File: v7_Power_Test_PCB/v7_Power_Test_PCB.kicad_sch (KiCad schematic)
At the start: 0 parts

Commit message: update fuel gauge
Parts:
- added BT101, BT102: Battery_Cell, symbol Device:Battery_Cell
- added C1001, C101, C102, C105, C107, C108, C133, C136, C139: 0.1u, symbol Device:C
- added C1002, C114, C115, C126, C128: 1u, symbol Device:C
- added C1003: 10n, symbol Device:C
- added C104, C109: 4.3n, symbol Device:C
- added C110, C113, C122, C123: 100n, symbol Device:C
- added C111, C112, C125: 10u, symbol Device:C
- added C116: 100nF, symbol Device:C
- added C117, C118, C121, C129, C130, C131, C140: 47u, symbol Device:C
- added C119: 47p, symbol Device:C
- added C120: 1n, symbol Device:C
- added C124: 330u, symbol Device:C
- added C127: 4.7u, symbol Device:C
- added C132: 560u, symbol Device:C
- added C134: 150p, symbol Device:C
- added C135: 18n, symbol Device:C
- added C137, C138: 22u, symbol Device:C
- added D101, D102: D_TVS, ESD5451N2:DFN1006-2L_TWS, symbol Device:D_TVS
- added J101: Conn_01x02_Pin, symbol Connector:Conn_01x02_Pin
- added L101: 1u, symbol Device:L
- added L102: 4.7u, symbol Device:L
- added L103: 220n, symbol Device:L
- added R1001: 10m, symbol Device:R
- added R101, R102, R120, R121, R129, R130, R134, R142, R149, R150: 0, symbol Device:R
- added R106, R122: 470k, symbol Device:R
- added R107, R123: 47k, symbol Device:R
- added R110, R124: 82.5k, symbol Device:R
- added R111, R125: 27.4k, symbol Device:R
- added R112, R126, R136: 10k, symbol Device:R
- added R113, R127, R152: 205k, symbol Device:R
- added R115, R128: 576, symbol Device:R
- added R131: 267k, symbol Device:R
- added R132: 8.2k, symbol Device:R
- added R133, R138: 5k, symbol Device:R
- added R135: 24k, symbol Device:R
- added R137: 220k, symbol Device:R
- added R139: 23.7k, symbol Device:R
- added R140: 69.8k, symbol Device:R
- added R141: 124k, symbol Device:R
- added R143: 162k, symbol Device:R
- added R144: 102k, symbol Device:R
- added R145: 24.9k, symbol Device:R
- added R146, R151: 100k, symbol Device:R
- added R147: 9.53k, symbol Device:R
- added R148: 12.1k, symbol Device:R
- added TH1001: Thermistor_NTC, Resistor_SMD:R_0201_0603Metric_Pad0.64x0.40mm_HandSolder, symbol Device:Thermistor_NTC
- added U1001: ~, Package_DFN_QFN:WDFN-12-1EP_3x3mm_P0.45mm_EP1.7x2.5mm, symbol RT9426:RT9426GQW
- added U101, U107, U112, U114: LTC4450AV-TRMPBF, LTC4450:05-08-1683_ADI, symbol LTC4450:LTC4450AV-TRMPBF
- added U102, U108: TPS22811LRPWR, TPS22811:IC_TPS22811LRPWR, symbol TPS22811LRPWR:TPS22811LRPWR
- added U103: SN74LVC1G32DBVR, SN74LVC1G32DBVR:SOT95P280X145-5N, symbol SN74LVC1G32DBVR:SN74LVC1G32DBVR
- added U105: SN74LVC1G14DBVR, SN74LVC1G14DBVR:SOT95P280X145-5N, symbol SN74LVC1G14DBVR:SN74LVC1G14DBVR
- added U106: SN74LVC1G08DBVR, SN74LVC1G08DBVR:SOT95P280X145-5N, symbol SN74LVC1G08DBVR:SN74LVC1G08DBVR
- added U109: TPS2121RUXR, TPS2121RUXR:RUX0012A, symbol TPS2121RUXR:TPS2121RUXR
- added U110: TPS61088RHLR, TPS61088RHLR:IC_TPS61088RHLR, symbol TPS61088RHLR:TPS61088RHLR
- added U111: XTPS55285VALR, TPS55285VALR:VAL0015A, symbol TPS55285VALR:XTPS55285VALR
- added U113: TPS62867RQYR, TPS62867RQYR:RQY0009A-MFG, symbol TPS62867RQYR:TPS62867RQYR
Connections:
- new net: C128.1, C129.1, C130.1, C131.1, C132.1, R144.2, U111.9 (VOUT), U112.16 (SHDN#), U112.2 (IN), U112.3 (IN), U112.4 (IN), U112.5 (IN), U112.6 (IN), U112.7 (IN)
- new net: R145.2, U111.1 (MODE)
- new net: R121.1, U107.10 (OUT), U107.11 (OUT), U107.12 (OUT), U107.13 (OUT), U107.8 (OUT), U107.9 (OUT)
- new net: R137.2, R140.1, U110.17 (FB)
- new net: R150.1, U114.10 (OUT), U114.11 (OUT), U114.12 (OUT), U114.13 (OUT), U114.8 (OUT), U114.9 (OUT)
- new net: R143.2, R146.1, U111.4 (EN_UVLO)
- new net: R101.2, R106.1, U102.5 (IN)
- new net: R106.2, R110.1, U102.1 (EN/UVLO)
- new net: R120.2, R122.1, U108.5 (IN)
- new net: R122.2, R124.1, U108.1 (EN/UVLO)
- new net: C114.1, C115.1, U110.1 (VCC)
- new net: C110.2, L101.2, R131.1, U110.4 (SW_7), U110.5 (SW_4), U110.6 (SW_5), U110.7 (SW_6)
- new net: R131.2, U110.3 (FSW)
- new net: R110.2, R113.1, U102.2 (~{EN}/OVLO)
- new net: R123.2, R125.1, U108.4 (PGTH)
- new net: C127.1, U111.13 (VCC)
- new net: R128.1, U108.9 (IMON)
- new net: C134.1, R148.2, U111.11 (COMP)
- new net: BT102.1 (+), R120.1
- new net: R144.1, R147.2, U111.10 (FB_INT_N)
- new net: C1003.1, TH1001.1, U1001.5 (VPTS)
- new net: C1003.2, TH1001.2, U1001.9 (TS)
- new net: BT101.1 (+), R101.1
- new net: C119.1, R139.1, U110.18 (COMP)
- new net: R102.1, U101.10 (OUT), U101.11 (OUT), U101.12 (OUT), U101.13 (OUT), U101.8 (OUT), U101.9 (OUT)
- new net: R149.2, R151.1, U113.3 (VIN), U113.4 (EN)
- new net: R134.2, U109.2 (IN2)
- new net: R152.1, U113.6 (VSET_MODE)
- new net: C110.1, U110.8 (BOOT)
- new net: C104.1, U102.7 (DVDT)
- new net: C135.1, R148.1
- new net: C133.1, R142.1, U112.10 (OUT), U112.11 (OUT), U112.12 (OUT), U112.13 (OUT), U112.8 (OUT), U112.9 (OUT)
- new net: L103.1, U113.7 (SW)
- new net: R124.2, R127.1, U108.2 (~{EN}/OVLO)
- new net: C109.1, U108.7 (DVDT)
- new net: C123.1, L102.2, U111.8 (SW2)
- new net: C123.2, U111.14 (BOOT2)
- new net: C120.1, R139.2
- new net: C122.2, U111.15 (BOOT1)
- new net: C122.1, L102.1, U111.6 (SW1)
- new net: R130.1, U109.1 (OUT), U109.8 (OUT)
- new net: R135.1, U109.10 (ILM)
- new net: C116.1, U109.11 (SS)
- new net: R129.2, U109.7 (IN1)
- new net: U105.4 (Y), U106.1 (A)
- new net: R141.1, U110.19 (ILIM)
- new net: R107.2, R111.1, U102.4 (PGTH)
- new net: C121.1, U110.10 (SS)
- new net: R115.1, U102.9 (IMON)
- new net 5V_IN: C140.1, J101.1 (Pin_1), R129.1, R132.2, R149.1
- new net 5V_MUX_STATUS: U109.9 (ST)
- new net BATTERY_PACK_OUT: C1001.1, C1002.1, C102.1, C105.1, C108.1, C111.1, C112.1, C113.1, C124.1, C125.1, C126.1, L101.1, R102.2, R121.2, U1001.3 (VDD/VBAT), U1001.4 (VBATS), U103.5 (VCC), U110.9 (VIN), U111.5 (VIN)
- new net BATTERY_PG: U103.4, U106.2 (B), U110.2 (EN)
- new net BAT_3V3_EN: R143.1, U106.4 (Y)
- new net BAT_5V: C117.1, C118.1, R134.1, R136.1, R137.1, U110.14 (VOUT_16), U110.15 (VOUT_14), U110.16 (VOUT_15)
- new net CP2: R136.2, R138.2, U109.3 (CP2)
- new net ETH_3V3: C137.1, C138.1, C139.1, L103.2, U113.8 (VOS), U113.9 (FB), U114.16 (SHDN#), U114.2 (IN), U114.3 (IN), U114.4 (IN), U114.5 (IN), U114.6 (IN), U114.7 (IN)
- new net ETH_3V3_PG: R151.2, U105.2 (A), U113.5 (PG)
- new net FUEL_GAUGE_ALERT: U1001.12 (nALERT)
- new net FUEL_GAUGE_SCL: U1001.11 (SCL)
- new net FUEL_GAUGE_SDA: U1001.10 (SDA)
- new net GND: C1001.2, C111.2, C112.2, C113.2, C114.2, C115.2, C116.2, C117.2, C118.2, C119.2, C120.2, C121.2, C124.2, C125.2, C126.2, C127.2, C128.2, C129.2, C130.2, C131.2, C132.2, C133.2, C134.2, C135.2, C136.2, C137.2, C138.2, C139.2, C140.2, J101.2 (Pin_2), R1001.2, R133.2, R135.2, R138.1, R140.2, R141.2, R145.1, R146.2, R147.1, R152.2, U1001.6 (VSS), U1001.8 (CSN), U1001.EP, U103.3 (GND), U105.3 (GND), U106.3 (GND), U109.12 (GND), U109.4 (OV2), U109.5 (OV1), U110.11 (NC_11), U110.20 (AGND), U110.21 (PGND), U110.22 (PGND__1), U110.23 (PGND__2), U110.24 (PGND__3), U110.25 (PGND__4), U110.26 (PGND__5), U110.27 (PGND__6), U110.28 (PGND__7), U110.29 (PGND__8), U111.12 (AGND), U111.7 (PGND), U112.1 (VCC), U112.14 (GND), U112.15 (STATUS), U113.1 (AGND), U113.2 (PGND), U114.1 (VCC), U114.14 (GND), U114.15 (STATUS)
- new net LOAD_OUT_1: C101.1, D101.2 (A2), R107.1, R112.1, U101.16 (SHDN#), U101.2 (IN), U101.3 (IN), U101.4 (IN), U101.5 (IN), U101.6 (IN), U101.7 (IN), U102.6 (OUT)
- new net LOAD_OUT_2: C107.1, D102.2 (A2), R123.1, R126.1, U107.16 (SHDN#), U107.2 (IN), U107.3 (IN), U107.4 (IN), U107.5 (IN), U107.6 (IN), U107.7 (IN), U108.6 (OUT)
- new net LOAD_PG_1: R112.2, U102.3 (PG), U103.1
- new net LOAD_PG_2: R126.2, U103.2, U108.3 (PG)
- new net PACK_GND: BT101.2 (-), BT102.2 (-), C1002.2, C101.2, C102.2, C104.2, C105.2, C107.2, C108.2, C109.2, D101.1 (A1), D102.1 (A1), R1001.1, R111.2, R113.2, R115.2, R125.2, R127.2, R128.2, U1001.2 (VBATG), U1001.7 (CSP), U101.1 (VCC), U101.14 (GND), U101.15 (STATUS), U102.8 (GND), U107.1 (VCC), U107.14 (GND), U107.15 (STATUS), U108.8 (GND)
- new net PR1: R132.1, R133.1, U109.6 (PR1)
- new net VCC3V3_SYS: C136.1, R142.2, R150.2, U105.5 (VCC), U106.5 (VCC)
- new net VCC5V_SYS: R130.2
- no-connect marks 0 -> 1
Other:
- note added: "5V Boost EN when good battery"
- note added: "AND"
- note added: "Battery 3.3V Buck EN when good battery and no POE"
- note added: "Battery Management"
- note added: "Battery to 3.3V"
- note added: "Battery to 5V"
- note added: "Battery/Ethernet 5V Switchover"
- note added: "ESP FOR READING FUEL GAUGE"
- note added: "NOT"
- note added: "NOTE: CHECK FOOTPRINT DIMENSIONS W DATASHEET"
- note added: "PoE to 3.3V"
- note added: "Power Sequencing/EN Logic"
- note added: "RESISTORS FOR LOAD SIMULATION"
- note added: "STATUS indication unused"

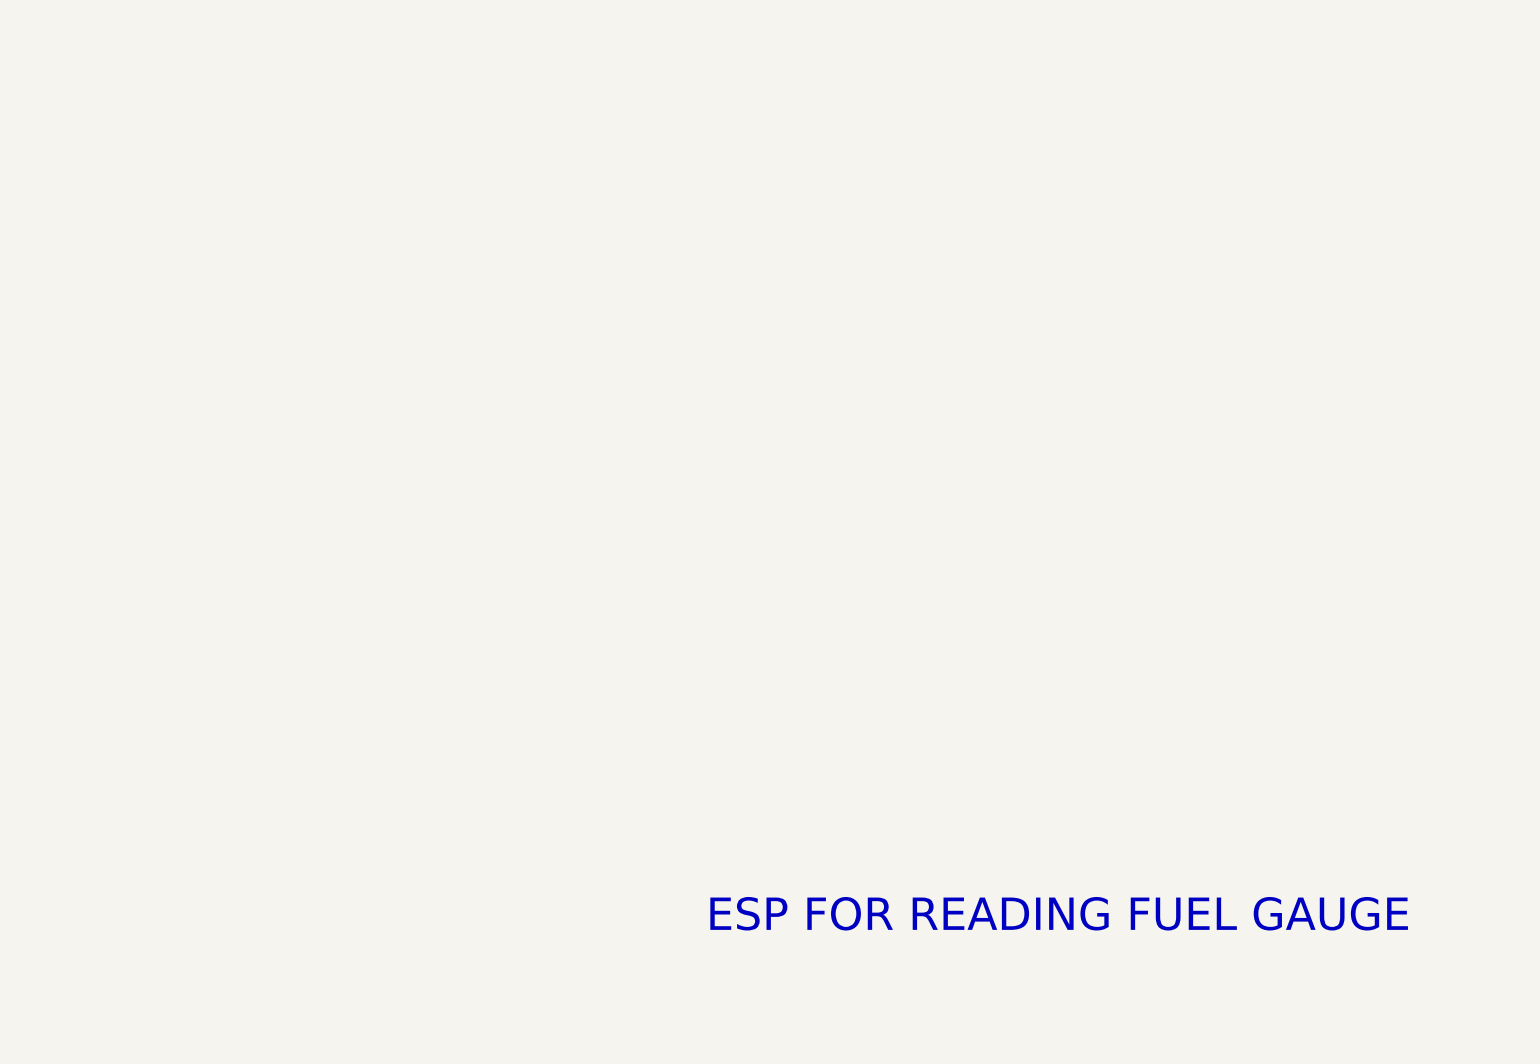
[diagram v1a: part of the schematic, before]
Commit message: add ESP32
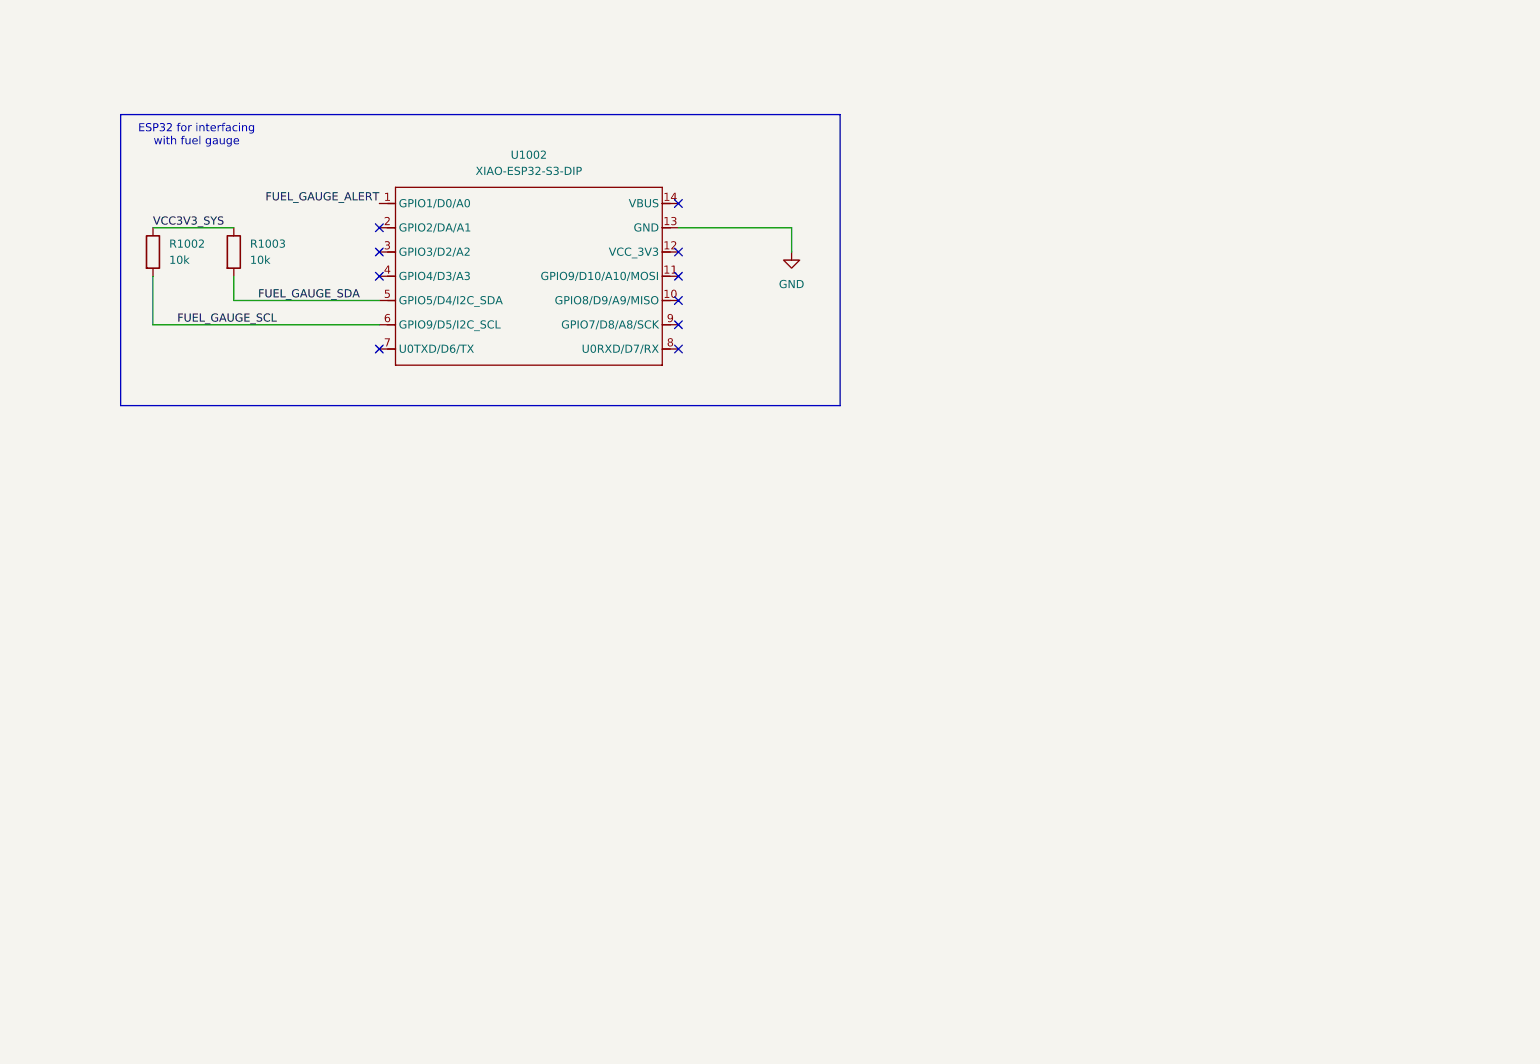
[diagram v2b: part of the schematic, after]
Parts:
- added R1002, R1003: 10k, symbol Device:R
- added U1002: XIAO-ESP32-S3-DIP, XIAO-ESP32S3:XIAO-ESP32S3-DIP, symbol XIAOESP32S3S:XIAO-ESP32-S3-DIP
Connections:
- net FUEL_GAUGE_ALERT: now also U1002.1 (GPIO1/D0/A0)
- net FUEL_GAUGE_SCL: now also R1002.2, U1002.6 (GPIO9/D5/I2C_SCL)
- net FUEL_GAUGE_SDA: now also R1003.2, U1002.5 (GPIO5/D4/I2C_SDA)
- net GND: now also U1002.13 (GND)
- net VCC3V3_SYS: now also R1002.1, R1003.1
- no-connect marks 1 -> 11
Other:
- note added: "ESP32 for interfacing with fuel gauge"
- note removed: "ESP FOR READING FUEL GAUGE"

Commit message: finish schematic and footprint assignments
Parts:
- removed BT101, BT102: Battery_Cell, symbol Device:Battery_Cell
- removed C124: 330u, symbol Device:C
- added BT1, BT2, BT3, BT4: 246, 246:BAT_246, symbol 246:246
- added C1, C10, C11, C2: 100n, Capacitor_SMD:C_0603_1608Metric_Pad1.08x0.95mm_HandSolder, symbol Device:C
- added C29: 330u, UCD0J331MCL1GS:PCAP_6.3x7.7-ELECT_NCA, symbol Device:C_Polarized_US
- added R35, R43: 50, Resistor_SMD:R_1206_3216Metric_Pad1.30x1.75mm_HandSolder, symbol Device:R
- added R36, R37, R38: AP725 5R F, AP725_5R_F:RES_AP725_OHM, symbol AP725_5R_F:AP725_5R_F
- added R39, R40, R41, R42: 3.3, CPA2512Q3R30FS_T10:RES_2512_SUS, symbol Device:R
- C12: renamed from C107; value 0.1u -> 100n; footprint (none) -> Capacitor_SMD:C_0603_1608Metric_Pad1.08x0.95mm_HandSolder
- C13: renamed from C108; value 0.1u -> 100n; footprint (none) -> Capacitor_SMD:C_0603_1608Metric_Pad1.08x0.95mm_HandSolder
- C14: renamed from C109; footprint (none) -> Capacitor_SMD:C_0603_1608Metric_Pad1.08x0.95mm_HandSolder
- C15: renamed from C110; footprint (none) -> Capacitor_SMD:C_0603_1608Metric_Pad1.08x0.95mm_HandSolder
- C16: renamed from C111; footprint (none) -> Capacitor_SMD:C_0603_1608Metric_Pad1.08x0.95mm_HandSolder
- C17: renamed from C112; footprint (none) -> Capacitor_SMD:C_0603_1608Metric_Pad1.08x0.95mm_HandSolder
- C18: renamed from C113; footprint (none) -> Capacitor_SMD:C_0603_1608Metric_Pad1.08x0.95mm_HandSolder
- C19: renamed from C114; footprint (none) -> Capacitor_SMD:C_0603_1608Metric_Pad1.08x0.95mm_HandSolder
- C20: renamed from C115; footprint (none) -> Capacitor_SMD:C_0603_1608Metric_Pad1.08x0.95mm_HandSolder
- C21: renamed from C116; value 100nF -> 100n; footprint (none) -> Capacitor_SMD:C_0603_1608Metric_Pad1.08x0.95mm_HandSolder
- C22: renamed from C117; footprint (none) -> Capacitor_SMD:C_0603_1608Metric_Pad1.08x0.95mm_HandSolder
- C23: renamed from C118; footprint (none) -> Capacitor_SMD:C_0603_1608Metric_Pad1.08x0.95mm_HandSolder
- C24: renamed from C119; footprint (none) -> Capacitor_SMD:C_0603_1608Metric_Pad1.08x0.95mm_HandSolder
- C25: renamed from C120; footprint (none) -> Capacitor_SMD:C_0603_1608Metric_Pad1.08x0.95mm_HandSolder
- C26: renamed from C121; footprint (none) -> Capacitor_SMD:C_0603_1608Metric_Pad1.08x0.95mm_HandSolder
- C27: renamed from C122; footprint (none) -> Capacitor_SMD:C_0603_1608Metric_Pad1.08x0.95mm_HandSolder
- C28: renamed from C123; footprint (none) -> Capacitor_SMD:C_0603_1608Metric_Pad1.08x0.95mm_HandSolder
- C3: renamed from C101; value 0.1u -> 100n; footprint (none) -> Capacitor_SMD:C_0603_1608Metric_Pad1.08x0.95mm_HandSolder
- C30: renamed from C125; footprint (none) -> Capacitor_SMD:C_0603_1608Metric_Pad1.08x0.95mm_HandSolder
- C31: renamed from C126; footprint (none) -> Capacitor_SMD:C_0603_1608Metric_Pad1.08x0.95mm_HandSolder
- C32: renamed from C127; footprint (none) -> Capacitor_SMD:C_0603_1608Metric_Pad1.08x0.95mm_HandSolder
- C33: renamed from C128; footprint (none) -> Capacitor_SMD:C_0603_1608Metric_Pad1.08x0.95mm_HandSolder
- C34: renamed from C129; footprint (none) -> Capacitor_SMD:C_0603_1608Metric_Pad1.08x0.95mm_HandSolder
- C35: renamed from C130; footprint (none) -> Capacitor_SMD:C_0603_1608Metric_Pad1.08x0.95mm_HandSolder
- C36: renamed from C131; footprint (none) -> Capacitor_SMD:C_0603_1608Metric_Pad1.08x0.95mm_HandSolder
- C37: renamed from C132; footprint (none) -> 16SVPF560M:CAP_16SVPF560M
- C38: renamed from C133; value 0.1u -> 100n; footprint (none) -> Capacitor_SMD:C_0603_1608Metric_Pad1.08x0.95mm_HandSolder
- C39: renamed from C134; footprint (none) -> Capacitor_SMD:C_0603_1608Metric_Pad1.08x0.95mm_HandSolder
- C4: renamed from C102; value 0.1u -> 100n; footprint (none) -> Capacitor_SMD:C_0603_1608Metric_Pad1.08x0.95mm_HandSolder
- C40: renamed from C135; footprint (none) -> Capacitor_SMD:C_0603_1608Metric_Pad1.08x0.95mm_HandSolder
- C41: renamed from C136; value 0.1u -> 100n; footprint (none) -> Capacitor_SMD:C_0603_1608Metric_Pad1.08x0.95mm_HandSolder
- C42: renamed from C137; footprint (none) -> Capacitor_SMD:C_0603_1608Metric_Pad1.08x0.95mm_HandSolder
- C43: renamed from C138; footprint (none) -> Capacitor_SMD:C_0603_1608Metric_Pad1.08x0.95mm_HandSolder
- C44: renamed from C139; value 0.1u -> 100n; footprint (none) -> Capacitor_SMD:C_0603_1608Metric_Pad1.08x0.95mm_HandSolder
- C45: renamed from C140; footprint (none) -> Capacitor_SMD:C_0603_1608Metric_Pad1.08x0.95mm_HandSolder
- C5: renamed from C1001; value 0.1u -> 100n; footprint (none) -> Capacitor_SMD:C_0603_1608Metric_Pad1.08x0.95mm_HandSolder
- C6: renamed from C105; value 0.1u -> 100n; footprint (none) -> Capacitor_SMD:C_0603_1608Metric_Pad1.08x0.95mm_HandSolder
- C7: renamed from C1003; footprint (none) -> Capacitor_SMD:C_0603_1608Metric_Pad1.08x0.95mm_HandSolder
- C8: renamed from C1002; footprint (none) -> Capacitor_SMD:C_0603_1608Metric_Pad1.08x0.95mm_HandSolder
- C9: renamed from C104; footprint (none) -> Capacitor_SMD:C_0603_1608Metric_Pad1.08x0.95mm_HandSolder
- J1: renamed from J101; footprint (none) -> Connector_PinHeader_2.54mm:PinHeader_1x02_P2.54mm_Horizontal
- L1: renamed from L101; footprint (none) -> BMRF001010401R0MD1:IND_BMRF001010401_PUL
- L2: renamed from L102; footprint (none) -> ETQ_P4M4R7KVC:IND_PCC-M1040LP_PAN
- L3: renamed from L103; footprint (none) -> IHLP2020CZERR22M8A:IND_IHLP-2020CZ-8A_VIS
- R1: renamed from R101; footprint (none) -> Resistor_SMD:R_0805_2012Metric_Pad1.20x1.40mm_HandSolder
- R10: renamed from R1001; footprint (none) -> Resistor_SMD:R_2512_6332Metric_Pad1.40x3.35mm_HandSolder
- R11: renamed from R120; footprint (none) -> Resistor_SMD:R_0805_2012Metric_Pad1.20x1.40mm_HandSolder
- R12: renamed from R121; footprint (none) -> Resistor_SMD:R_0805_2012Metric_Pad1.20x1.40mm_HandSolder
- R13: renamed from R122; footprint (none) -> Resistor_SMD:R_0603_1608Metric_Pad0.98x0.95mm_HandSolder
- R14: renamed from R123; footprint (none) -> Resistor_SMD:R_0603_1608Metric_Pad0.98x0.95mm_HandSolder
- R15: renamed from R124; footprint (none) -> Resistor_SMD:R_0603_1608Metric_Pad0.98x0.95mm_HandSolder
- R16: renamed from R125; footprint (none) -> Resistor_SMD:R_0603_1608Metric_Pad0.98x0.95mm_HandSolder
- R17: renamed from R126; footprint (none) -> Resistor_SMD:R_0603_1608Metric_Pad0.98x0.95mm_HandSolder
- R18: renamed from R127; footprint (none) -> Resistor_SMD:R_0603_1608Metric_Pad0.98x0.95mm_HandSolder
- R19: renamed from R128; footprint (none) -> Resistor_SMD:R_0603_1608Metric_Pad0.98x0.95mm_HandSolder
- R2: renamed from R102; footprint (none) -> Resistor_SMD:R_0805_2012Metric_Pad1.20x1.40mm_HandSolder
- R20: renamed from R1002; footprint (none) -> Resistor_SMD:R_0603_1608Metric_Pad0.98x0.95mm_HandSolder
- R21: renamed from R1003; footprint (none) -> Resistor_SMD:R_0603_1608Metric_Pad0.98x0.95mm_HandSolder
- R22: renamed from R129; footprint (none) -> Resistor_SMD:R_0805_2012Metric_Pad1.20x1.40mm_HandSolder
- R23: renamed from R130; footprint (none) -> Resistor_SMD:R_0805_2012Metric_Pad1.20x1.40mm_HandSolder
- R24: renamed from R131; footprint (none) -> Resistor_SMD:R_0603_1608Metric_Pad0.98x0.95mm_HandSolder
- R25: renamed from R132; footprint (none) -> Resistor_SMD:R_0603_1608Metric_Pad0.98x0.95mm_HandSolder
- R26: renamed from R133; footprint (none) -> Resistor_SMD:R_0603_1608Metric_Pad0.98x0.95mm_HandSolder
- R27: renamed from R134; footprint (none) -> Resistor_SMD:R_0805_2012Metric_Pad1.20x1.40mm_HandSolder
- R28: renamed from R135; footprint (none) -> Resistor_SMD:R_0603_1608Metric_Pad0.98x0.95mm_HandSolder
- R29: renamed from R136; footprint (none) -> Resistor_SMD:R_0603_1608Metric_Pad0.98x0.95mm_HandSolder
- R3: renamed from R106; footprint (none) -> Resistor_SMD:R_0603_1608Metric_Pad0.98x0.95mm_HandSolder
- R30: renamed from R137; footprint (none) -> Resistor_SMD:R_0603_1608Metric_Pad0.98x0.95mm_HandSolder
- R31: renamed from R138; footprint (none) -> Resistor_SMD:R_0603_1608Metric_Pad0.98x0.95mm_HandSolder
- R32: renamed from R139; footprint (none) -> Resistor_SMD:R_0603_1608Metric_Pad0.98x0.95mm_HandSolder
- R33: renamed from R140; footprint (none) -> Resistor_SMD:R_0603_1608Metric_Pad0.98x0.95mm_HandSolder
- R34: renamed from R141; footprint (none) -> Resistor_SMD:R_0603_1608Metric_Pad0.98x0.95mm_HandSolder
- R4: renamed from R107; footprint (none) -> Resistor_SMD:R_0603_1608Metric_Pad0.98x0.95mm_HandSolder
- R44: renamed from R142; footprint (none) -> Resistor_SMD:R_0805_2012Metric_Pad1.20x1.40mm_HandSolder
- R45: renamed from R143; footprint (none) -> Resistor_SMD:R_0603_1608Metric_Pad0.98x0.95mm_HandSolder
- R46: renamed from R144; footprint (none) -> Resistor_SMD:R_0603_1608Metric_Pad0.98x0.95mm_HandSolder
- R47: renamed from R145; footprint (none) -> Resistor_SMD:R_0603_1608Metric_Pad0.98x0.95mm_HandSolder
- R48: renamed from R146; footprint (none) -> Resistor_SMD:R_0603_1608Metric_Pad0.98x0.95mm_HandSolder
- R49: renamed from R147; footprint (none) -> Resistor_SMD:R_0603_1608Metric_Pad0.98x0.95mm_HandSolder
- R5: renamed from R110; footprint (none) -> Resistor_SMD:R_0603_1608Metric_Pad0.98x0.95mm_HandSolder
- R50: renamed from R148; footprint (none) -> Resistor_SMD:R_0603_1608Metric_Pad0.98x0.95mm_HandSolder
- R51: renamed from R149; footprint (none) -> Resistor_SMD:R_0805_2012Metric_Pad1.20x1.40mm_HandSolder
- R52: renamed from R150; footprint (none) -> Resistor_SMD:R_0805_2012Metric_Pad1.20x1.40mm_HandSolder
- R53: renamed from R151; footprint (none) -> Resistor_SMD:R_0603_1608Metric_Pad0.98x0.95mm_HandSolder
- R54: renamed from R152; footprint (none) -> Resistor_SMD:R_0603_1608Metric_Pad0.98x0.95mm_HandSolder
- R6: renamed from R111; footprint (none) -> Resistor_SMD:R_0603_1608Metric_Pad0.98x0.95mm_HandSolder
- R7: renamed from R112; footprint (none) -> Resistor_SMD:R_0603_1608Metric_Pad0.98x0.95mm_HandSolder
- R8: renamed from R113; footprint (none) -> Resistor_SMD:R_0603_1608Metric_Pad0.98x0.95mm_HandSolder
- R9: renamed from R115; footprint (none) -> Resistor_SMD:R_0603_1608Metric_Pad0.98x0.95mm_HandSolder
- renumbered D101 to D1, D102 to D2, TH1001 to TH1, U101 to U1, U109 to U10, U110 to U11, U111 to U12, U112 to U13, U113 to U14, U114 to U15, U102 to U2, U1001 to U3, U103 to U4, U105 to U5, U106 to U6, U107 to U7, U108 to U8, U1002 to U9
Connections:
- net 5V_MUX_STATUS: now also U9.2 (GPIO2/DA/A1)
- net BATTERY_PACK_OUT: now also C29.1
- net GND: now also C29.2, R35.2, R36.1, R37.1, R38.1, R39.2, R40.2, R41.2, R42.2, R43.2
- net PACK_GND: now also BT2.1_1, BT2.1_2, BT4.1_1, BT4.1_2, C1.2, C10.2, C11.2, C2.2
- net VCC3V3_SYS: now also R39.1, R40.1, R41.1, R42.1, R43.1
- net VCC5V_SYS: now also R37.2
- net at R1.2, R3.1, U2.5 (IN): now also C1.1, C2.1
- net at R11.2, R13.1, U8.5 (IN): now also C10.1, C11.1
- net at R11.1: now also BT3.1_1, BT3.1_2
- net at R1.1: now also BT1.1_1, BT1.1_2
- new net: R35.1, R36.2, R38.2
- no-connect marks 11 -> 10
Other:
- note added: "3.3V Load Simulation"
- note added: "3.3V Load Simulation with 3.3Ohm: 1 resistor = 1A 2 resistor = 2A 3 resistor = 3A To simulate low current load, populate only the 50Ohm"
- note added: "5V Load Simulation"
- note added: "5V Load Simulation with 5Ohm: 1 resistor = 1A 2 resistor = 2A 3 resistor = 3A To simulate low current load, populate only the 50Ohm"
- note removed: "RESISTORS FOR LOAD SIMULATION"
- note removed: "STATUS indication unused"
- moved on the sheet: C14, C9, D1, D2, R1, R11, R13, R14, R15, R16, R17, R18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
